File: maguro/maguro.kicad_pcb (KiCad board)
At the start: 2 copper layers, 114.3 x 69.8 mm, 23 parts, among them SW1001 SW_Push, SW1101 SW_Push, SW1301 SW_Push, SW1401 SW_Push, SW301 SW_Push, SW401 SW_Push, SW501 SW_Push, SW601 SW_Push, SW801 SW_Push, SW901 SW_Push

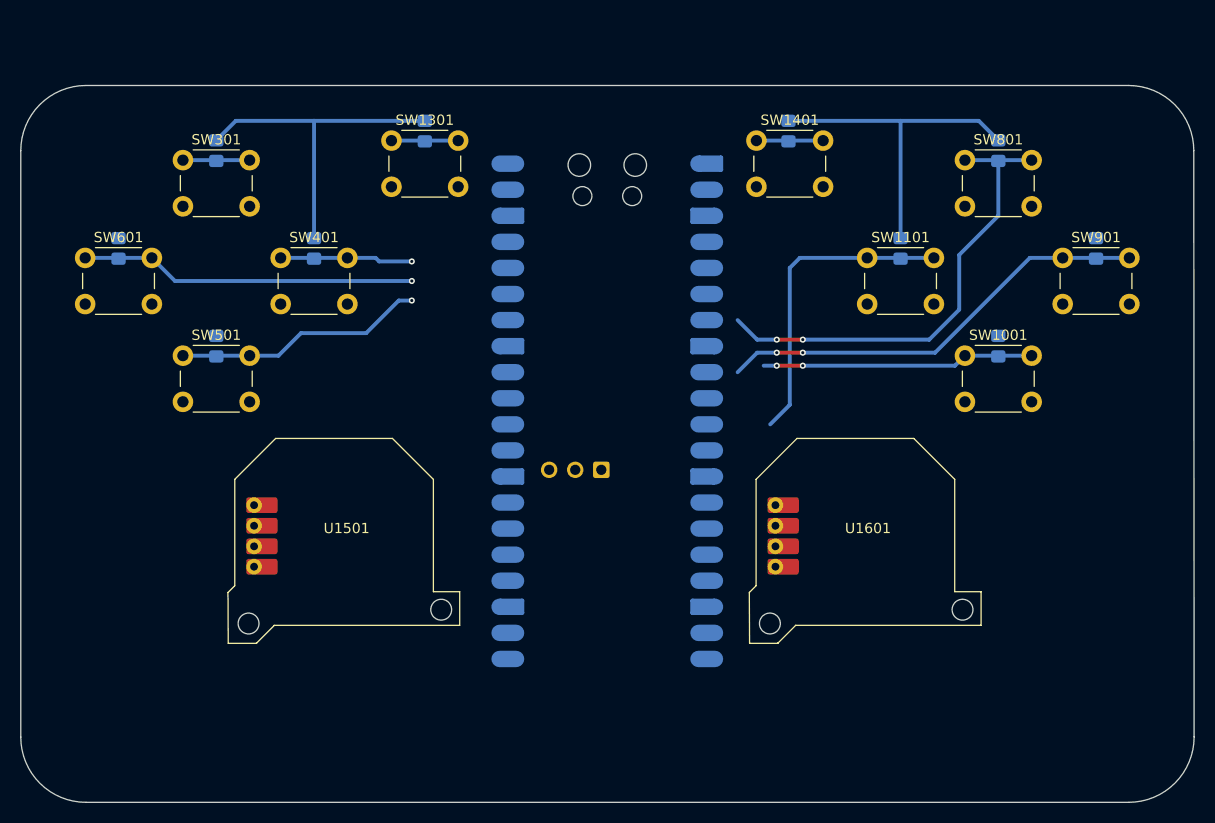
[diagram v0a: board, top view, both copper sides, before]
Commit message: Added silkscreen
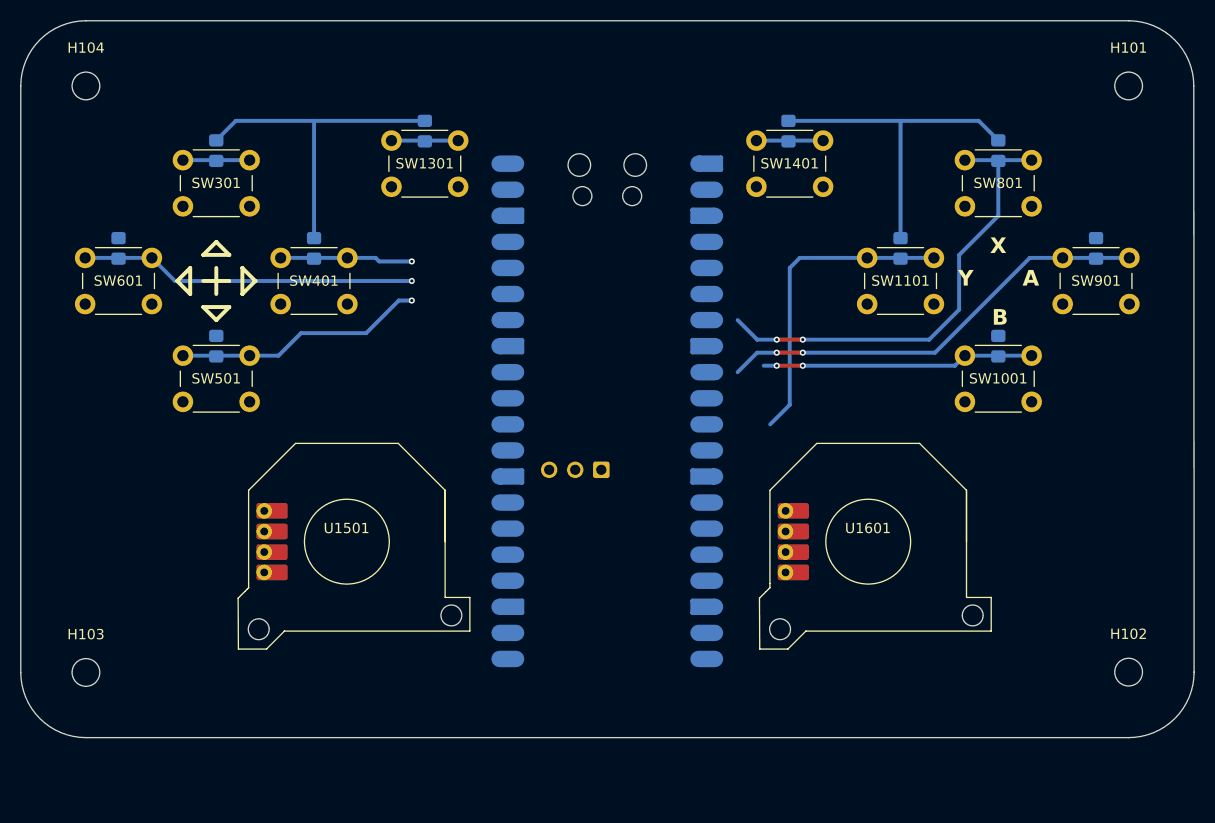
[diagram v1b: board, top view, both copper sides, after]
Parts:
- added H101: MountingHole, MountingHole:MountingHole_2.7mm_M2.5, F.Cu at (190.5, 69.9)
- added H102: MountingHole, MountingHole:MountingHole_2.7mm_M2.5, F.Cu at (190.5, 127.0)
- added H103: MountingHole, MountingHole:MountingHole_2.7mm_M2.5, F.Cu at (88.9, 127.0)
- added H104: MountingHole, MountingHole:MountingHole_2.7mm_M2.5, F.Cu at (88.9, 69.9)
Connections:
- U1501 pad 2: +5V -> +3V3
- U1601 pad 2: +5V -> +3V3
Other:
- board text added: "A"
- board text added: "B"
- board text added: "X"
- board text added: "Y"
